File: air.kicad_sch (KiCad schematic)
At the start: 31 parts, among them J1 Conn_01x05, J2 Conn_01x05, J3 Conn_01x04, U1 短接, U2 AIR32F103CBT6-LQFP48, U3 RT9013-33GB, U4 USBLC6-2SC6, Y1 8M/20pF

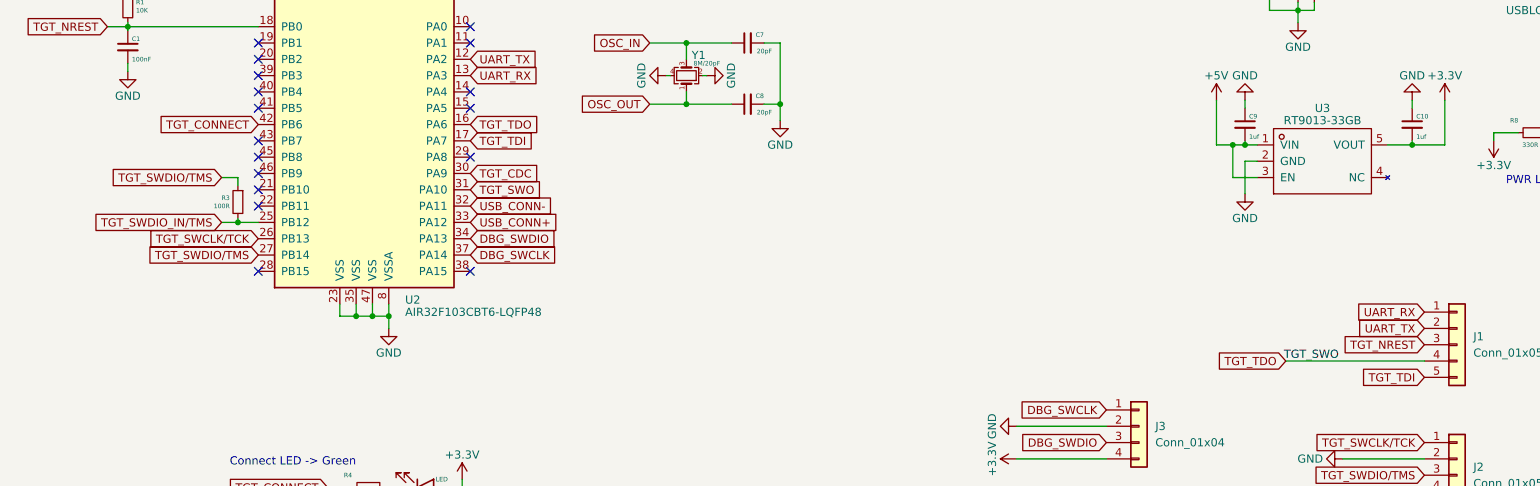
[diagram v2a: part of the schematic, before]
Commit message: v1.5 added series resistor on debug lines
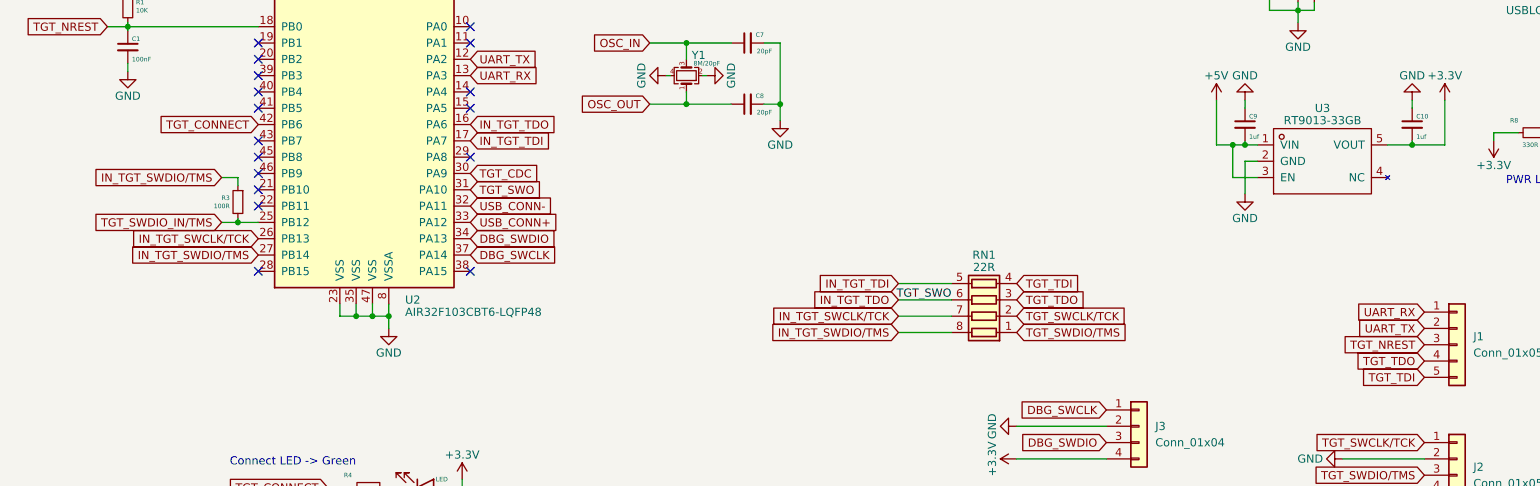
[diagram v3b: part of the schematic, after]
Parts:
- added RN1: 22R, Resistor_SMD:R_Array_Convex_4x0603, symbol Device:R_Pack04
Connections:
- net TGT_SWCLK/TCK: now also RN1.2 (R2.1); no longer U2.26 (PB13)
- net TGT_SWDIO/TMS: now also RN1.1 (R1.1); no longer R3.1, U2.27 (PB14)
- net TGT_TDI: now also RN1.4 (R4.1); no longer U2.17 (PA7)
- net TGT_SWO renamed IN_TGT_TDO
- net IN_TGT_TDO: now also RN1.6 (R3.2); no longer J1.4 (Pin_4)
- new net IN_TGT_SWCLK/TCK: RN1.7 (R2.2), U2.26 (PB13)
- new net IN_TGT_SWDIO/TMS: R3.1, RN1.8 (R1.2), U2.27 (PB14)
- new net IN_TGT_TDI: RN1.5 (R4.2), U2.17 (PA7)
- new net TGT_TDO: J1.4 (Pin_4), RN1.3 (R3.1)
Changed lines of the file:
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@@
+    (stroke (width 0) (type default) (color 0 0 0 0))
+  )
+  (wire (pts (xy 153.67 119.38) (xy 161.925 119.38))
     (stroke (width 0) (type default) (color 0 0 0 0))
   )
@@
     (stroke (width 0) (type default) (color 0 0 0 0))
   )
+  (wire (pts (xy 153.67 111.76) (xy 161.925 111.76))
+    (stroke (width 0) (type default) (color 0 0 0 0))
+  )
   (wire (pts (xy 64.77 143.51) (xy 68.58 143.51))
     (stroke (width 0) (type default) (color 0 0 0 0))
@@
     (stroke (width 0) (type default) (color 0 0 0 0))
   )
+  (wire (pts (xy 153.67 116.84) (xy 161.925 116.84))
+    (stroke (width 0) (type default) (color 0 0 0 0))
+  )
   (wire (pts (xy 203.2 90.17) (xy 203.2 83.185))
     (stroke (width 0) (type default) (color 0 0 0 0))
@@
     (stroke (width 0) (type default) (color 0 0 0 0))
   )
-  (wire (pts (xy 213.995 123.825) (xy 235.585 123.825))
-    (stroke (width 0) (type default) (color 0 0 0 0))
-  )
   (wire (pts (xy 108.585 51.435) (xy 108.585 52.705))
     (stroke (width 0) (type default) (color 0 0 0 0))
@@
   )
   (wire (pts (xy 71.755 36.83) (xy 74.295 36.83))
+    (stroke (width 0) (type default) (color 0 0 0 0))
+  )
+  (wire (pts (xy 153.67 114.3) (xy 161.925 114.3))
     (stroke (width 0) (type default) (color 0 0 0 0))
   )
@@
     (effects (font (size 1.27 1.27)) (justify left bottom))
   )
-  (label "TGT_SWO" (at 222.25 123.825 180)
+  (label "TGT_SWO" (at 161.925 114.3 180)
     (effects (font (size 1.27 1.27)) (justify right bottom))
   )
+  (global_label "TGT_SWCLK{slash}TCK" (shape input) (at 172.085 116.84 0) (fields_autoplaced)
+    (effects (font (size 1.27 1.27)) (justify left))
+    (property "Intersheet References" "${INTERSHEET_REFS}" (id 0) (at 189.7381 116.7606 0)
+      (effects (font (size 1.27 1.27)) (justify left) hide)
+    )
+  )
   (global_label "DBG_SWDIO" (shape input) (at 186.055 136.525 180) (fields_autoplaced)
     (effects (font (size 1.27 1.27)) (justify right))
@@
     (property "Intersheet References" "${INTERSHEET_REFS}" (id 0) (at 218.1738 141.5256 0)
       (effects (font (size 1.27 1.27)) (justify right) hide)
+    )
+  )
+  (global_label "TGT_SWDIO{slash}TMS" (shape input) (at 172.085 119.38 0) (fields_autoplaced)
+    (effects (font (size 1.27 1.27)) (justify left))
+    (property "Intersheet References" "${INTERSHEET_REFS}" (id 0) (at 189.4962 119.3006 0)
+      (effects (font (size 1.27 1.27)) (justify left) hide)
     )
   )
@@
     )
   )
-  (global_label "TGT_TDO" (shape input) (at 86.995 86.995 0) (fields_autoplaced)
+  (global_label "TGT_TDO" (shape input) (at 172.085 114.3 0) (fields_autoplaced)
     (effects (font (size 1.27 1.27)) (justify left))
-    (property "Intersheet References" "${INTERSHEET_REFS}" (id 0) (at 97.1491 86.9156 0)
+    (property "Intersheet References" "${INTERSHEET_REFS}" (id 0) (at 182.2391 114.2206 0)
+      (effects (font (size 1.27 1.27)) (justify left) hide)
+    )
+  )
+  (global_label "IN_TGT_TDO" (shape input) (at 86.995 86.995 0) (fields_autoplaced)
+    (effects (font (size 1.27 1.27)) (justify left))
+    (property "Intersheet References" "${INTERSHEET_REFS}" (id 0) (at 100.0519 86.9156 0)
       (effects (font (size 1.27 1.27)) (justify left) hide)
     )
@@
     )
   )
-  (global_label "TGT_TDO" (shape input) (at 213.995 123.825 180) (fields_autoplaced)
-    (effects (font (size 1.27 1.27)) (justify right))
-    (property "Intersheet References" "${INTERSHEET_REFS}" (id 0) (at 203.8409 123.7456 0)
+  (global_label "TGT_TDO" (shape input) (at 235.585 123.825 180) (fields_autoplaced)
+    (effects (font (size 1.27 1.27)) (justify right))
+    (property "Intersheet References" "${INTERSHEET_REFS}" (id 0) (at 225.4309 123.7456 0)
       (effects (font (size 1.27 1.27)) (justify right) hide)
     )
@@
     )
   )
+  (global_label "IN_TGT_SWDIO{slash}TMS" (shape input) (at 153.67 119.38 180) (fields_autoplaced)
+    (effects (font (size 1.27 1.27)) (justify right))
+    (property "Intersheet References" "${INTERSHEET_REFS}" (id 0) (at 133.3559 119.3006 0)
+      (effects (font (size 1.27 1.27)) (justify right) hide)
+    )
+  )
   (global_label "USB_CONN+" (shape input) (at 265.43 54.61 0) (fields_autoplaced)
     (effects (font (size 1.27 1.27)) (justify left))
@@
     )
   )
-  (global_label "TGT_SWDIO{slash}TMS" (shape input) (at 48.26 95.25 180) (fields_autoplaced)
-    (effects (font (size 1.27 1.27)) (justify right))
-    (property "Intersheet References" "${INTERSHEET_REFS}" (id 0) (at 30.8488 95.1706 0)
-      (effects (font (size 1.27 1.27)) (justify right) hide)
+  (global_label "IN_TGT_SWDIO{slash}TMS" (shape input) (at 48.26 95.25 180) (fields_autoplaced)
+    (effects (font (size 1.27 1.27)) (justify right))
+    (property "Intersheet References" "${INTERSHEET_REFS}" (id 0) (at 27.9459 95.1706 0)
+      (effects (font (size 1.27 1.27)) (justify right) hide)
+    )
+  )
+  (global_label "TGT_TDI" (shape input) (at 172.085 111.76 0) (fields_autoplaced)
+    (effects (font (size 1.27 1.27)) (justify left))
+    (property "Intersheet References" "${INTERSHEET_REFS}" (id 0) (at 181.5133 111.6806 0)
+      (effects (font (size 1.27 1.27)) (justify left) hide)
     )
   )
@@
     )
   )
-  (global_label "TGT_SWDIO{slash}TMS" (shape input) (at 53.975 107.315 180) (fields_autoplaced)
-    (effects (font (size 1.27 1.27)) (justify right))
-    (property "Intersheet References" "${INTERSHEET_REFS}" (id 0) (at 36.5638 107.2356 0)
+  (global_label "IN_TGT_TDO" (shape input) (at 153.67 114.3 180) (fields_autoplaced)
+    (effects (font (size 1.27 1.27)) (justify right))
+    (property "Intersheet References" "${INTERSHEET_REFS}" (id 0) (at 140.6131 114.2206 0)
+      (effects (font (size 1.27 1.27)) (justify right) hide)
+    )
+  )
+  (global_label "IN_TGT_SWDIO{slash}TMS" (shape input) (at 53.975 107.315 180) (fields_autoplaced)
+    (effects (font (size 1.27 1.27)) (justify right))
+    (property "Intersheet References" "${INTERSHEET_REFS}" (id 0) (at 33.6609 107.2356 0)
       (effects (font (size 1.27 1.27)) (justify right) hide)
     )
@@
     )
   )
-  (global_label "TGT_SWCLK{slash}TCK" (shape input) (at 53.975 104.775 180) (fields_autoplaced)
-    (effects (font (size 1.27 1.27)) (justify right))
-    (property "Intersheet References" "${INTERSHEET_REFS}" (id 0) (at 36.3219 104.6956 0)
+  (global_label "IN_TGT_SWCLK{slash}TCK" (shape input) (at 53.975 104.775 180) (fields_autoplaced)
+    (effects (font (size 1.27 1.27)) (justify right))
+    (property "Intersheet References" "${INTERSHEET_REFS}" (id 0) (at 33.419 104.6956 0)
       (effects (font (size 1.27 1.27)) (justify right) hide)
     )
@@
     )
   )
+  (global_label "IN_TGT_SWCLK{slash}TCK" (shape input) (at 153.67 116.84 180) (fields_autoplaced)
+    (effects (font (size 1.27 1.27)) (justify right))
+    (property "Intersheet References" "${INTERSHEET_REFS}" (id 0) (at 133.114 116.7606 0)
+      (effects (font (size 1.27 1.27)) (justify right) hide)
+    )
+  )
   (global_label "UART_TX" (shape input) (at 235.585 118.745 180) (fields_autoplaced)
     (effects (font (size 1.27 1.27)) (justify right))
@@
     )
   )
+  (global_label "IN_TGT_TDI" (shape input) (at 153.67 111.76 180) (fields_autoplaced)
+    (effects (font (size 1.27 1.27)) (justify right))
+    (property "Intersheet References" "${INTERSHEET_REFS}" (id 0) (at 141.3388 111.6806 0)
+      (effects (font (size 1.27 1.27)) (justify right) hide)
+    )
+  )
   (global_label "TGT_SWCLK{slash}TCK" (shape input) (at 235.585 136.525 180) (fields_autoplaced)
     (effects (font (size 1.27 1.27)) (justify right))
@@
     )
   )
-  (global_label "TGT_TDI" (shape input) (at 86.995 89.535 0) (fields_autoplaced)
+  (global_label "IN_TGT_TDI" (shape input) (at 86.995 89.535 0) (fields_autoplaced)
     (effects (font (size 1.27 1.27)) (justify left))
-    (property "Intersheet References" "${INTERSHEET_REFS}" (id 0) (at 96.4233 89.4556 0)
+    (property "Intersheet References" "${INTERSHEET_REFS}" (id 0) (at 99.3262 89.4556 0)
       (effects (font (size 1.27 1.27)) (justify left) hide)
     )
@@
     (pin "5")
     (pin "6")
+  )
+  (symbol (lib_id "Device:R_Pack04") (at 167.005 114.3 90) (unit 1)
+    (in_bom yes) (on_board yes)
+    (property "Reference" "RN1" (id 0) (at 167.005 107.315 90))
+    (property "Value" "22R" (id 1) (at 167.005 109.22 90))
+    (property "Footprint" "Resistor_SMD:R_Array_Convex_4x0603" (id 2) (at 167.005 107.315 90)
+      (effects (font (size 1.27 1.27)) hide)
+    )
+    (property "Datasheet" "~" (id 3) (at 167.005 114.3 0)
+      (effects (font (size 1.27 1.27)) hide)
+    )
+    (pin "1")
+    (pin "2")
+    (pin "3")
+    (pin "4")
+    (pin "5")
+    (pin "6")
+    (pin "7")
+    (pin "8")
   )
   (symbol (lib_id "power:+3.3V") (at 172.085 139.065 90) (unit 1)
@@
       (reference "R9") (unit 1) (value "1.5K") (footprint "Resistor_SMD:R_0603_1608Metric")
     )
+    (path "/344a4318-dce8-4131-b81b-9dcb847b9d56"
+      (reference "RN1") (unit 1) (value "22R") (footprint "Resistor_SMD:R_Array_Convex_4x0603")
+    )
     (path "/af739715-377a-4a07-b553-a006961ff34c"

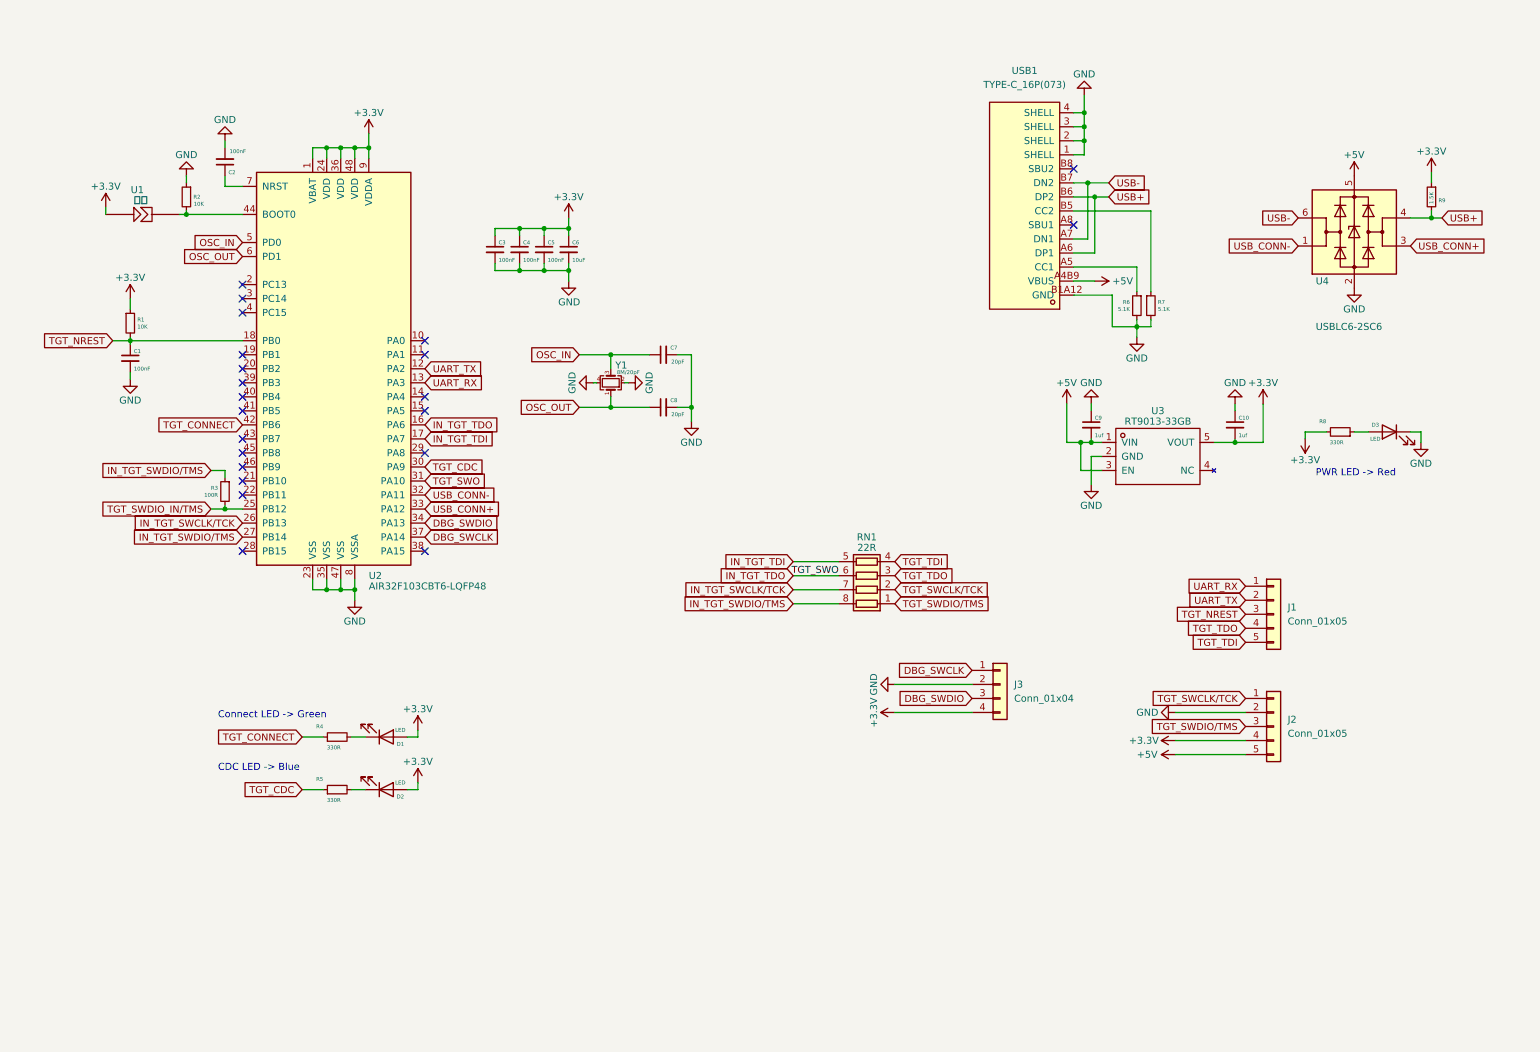
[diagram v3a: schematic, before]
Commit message: 1.6 Redesign And Add Anti Reverse Current
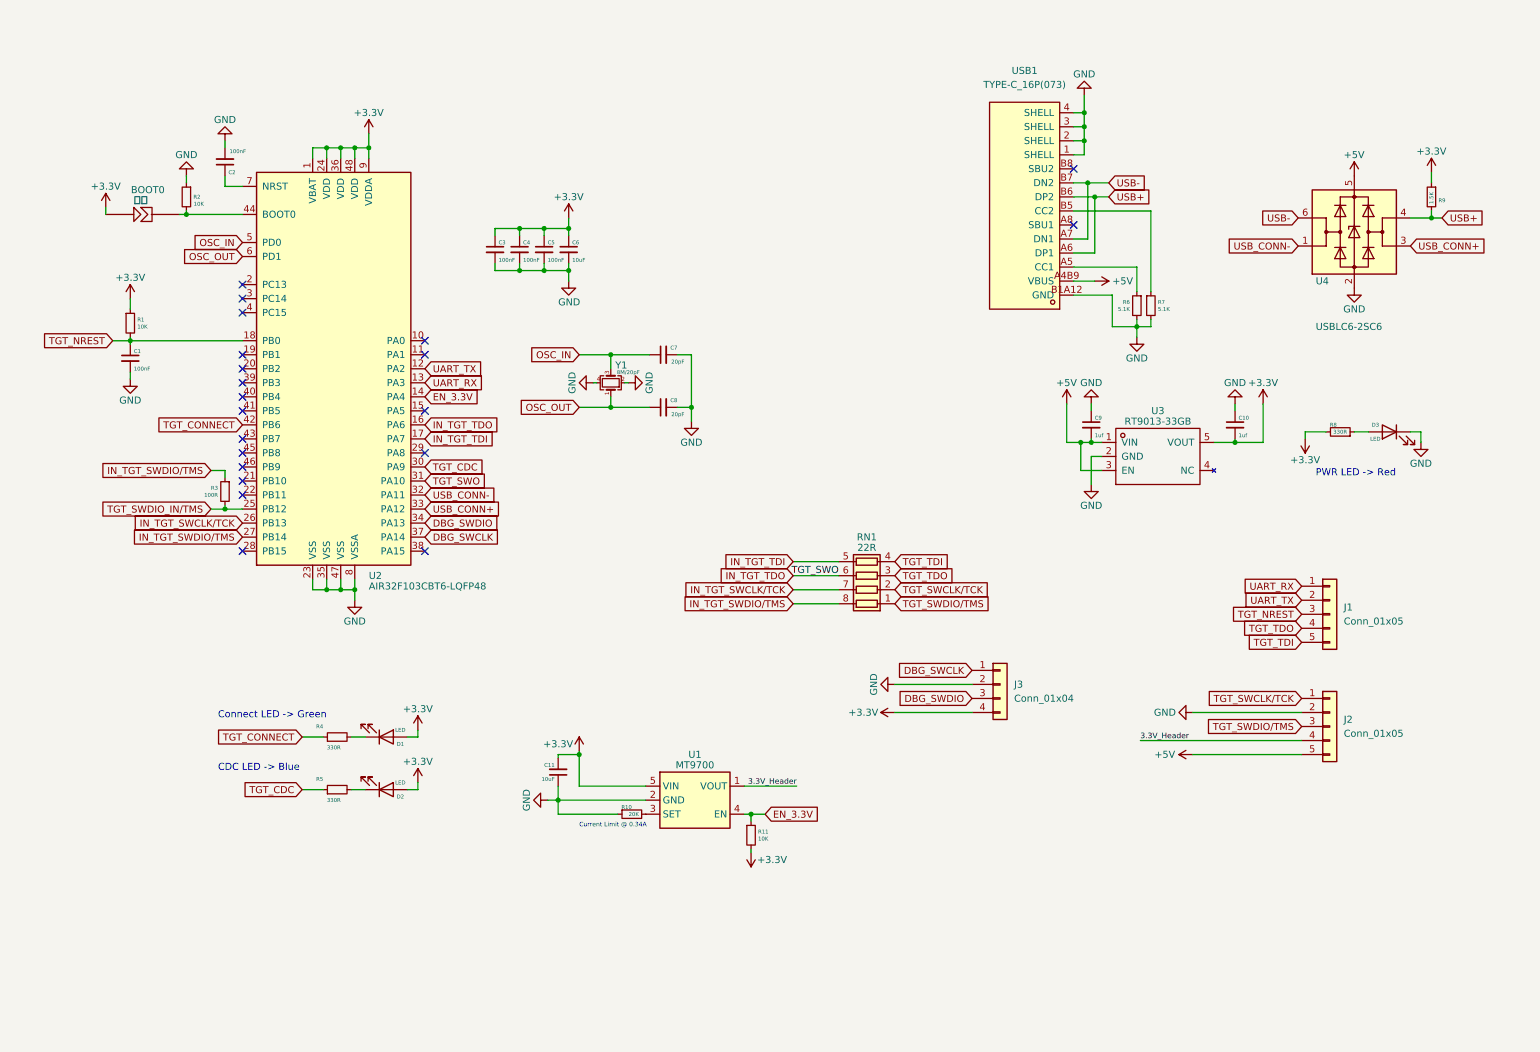
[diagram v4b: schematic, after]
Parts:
- added C11: 10uF, Capacitor_SMD:C_0603_1608Metric, symbol Device:C_Small
- added R10: 20K, Resistor_SMD:R_0603_1608Metric, symbol Device:R_Small
- added R11: 10K, Resistor_SMD:R_0603_1608Metric, symbol Device:R_Small
- added U1: MT9700, Package_TO_SOT_SMD:SOT-23-5, symbol Shaojie_Custom:MT9700
- U3: footprint Shaojie_Custom:SOT-23-5_L3.0-W1.7-P0.95-LS2.8-BR -> Package_TO_SOT_SMD:SOT-23-5
- renumbered U1 to BOOT0
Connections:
- net +3.3V: now also C11.2, R11.2, U1.5 (VIN); no longer J2.4 (Pin_4)
- net GND: now also C11.1, R10.1, U1.2 (GND)
- net EN_3.3V: now reaches U2.14 (PA4)
- net EN_3.3V: now also R11.1, U1.4 (EN)
- new net: R10.2, U1.3 (SET)
- new net 3.3V_Header: J2.4 (Pin_4), U1.1 (VOUT)
- no-connect marks 22 -> 21
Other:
- note added: "Current Limit @ 0.34A"
- moved on the sheet: J1, J2

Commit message: still 1.6 but contain some fix to publish work
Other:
- note added: "Current-Limited Power Switch"
- note added: "LDO"
- note added: "Lights"
- note added: "MCU Core"
- note added: "MCU Debug Port"
- note added: "Power IC"
- note added: "Target Debug Port"
- note added: "USB Port"
- company: (none) -> [REDACTED]
- title: (none) -> SWD WHISPERER
- moved on the sheet: BOOT0, C1, C10, C11, C2, C3, C4, C5, C6, C7, C8, C9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
